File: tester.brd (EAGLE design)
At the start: 56 x 67 mm, 73 parts, among them IC1 ATmega8/88/168, K1 NA 05W K, M1 SP6000C-180, P1 250, P2 10k lin, Q1 BC847CSMD, Q2 BC847CSMD, Q3 BC328-40, Q4 8,000 MHz, Q5 BC847CSMD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

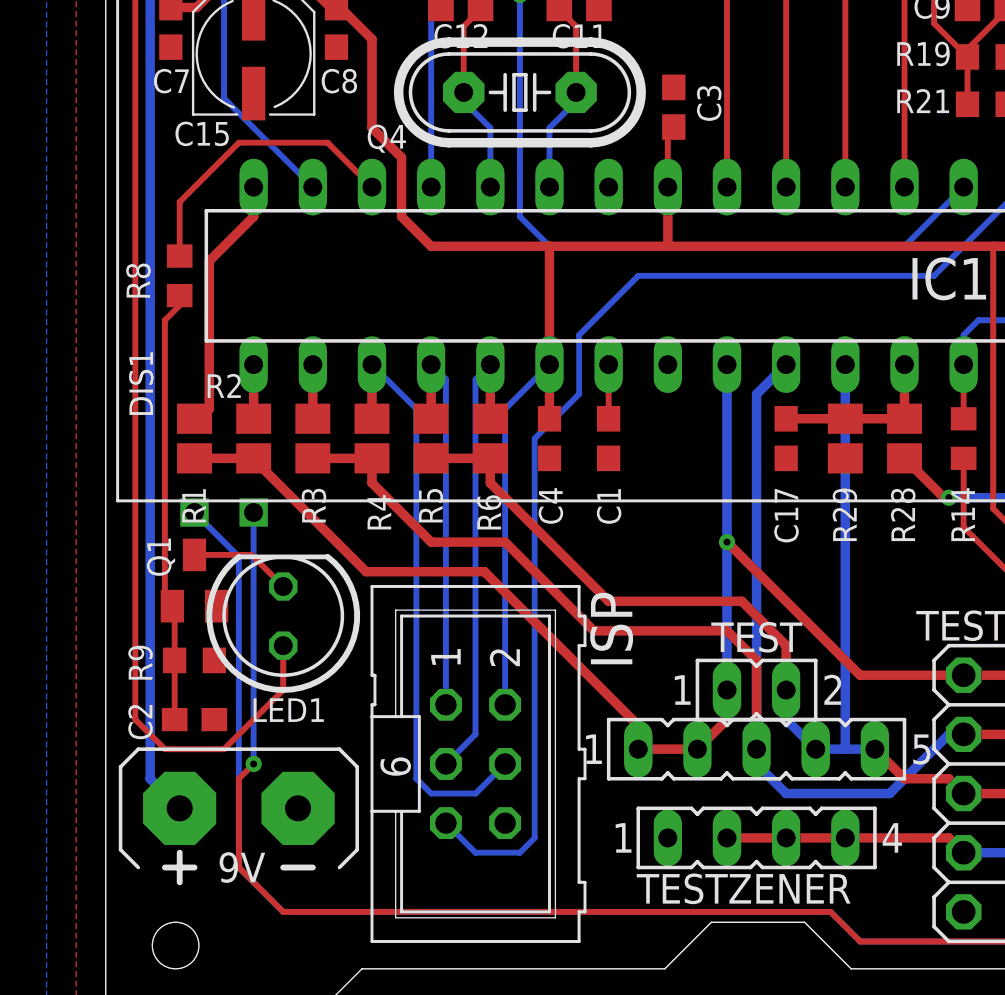
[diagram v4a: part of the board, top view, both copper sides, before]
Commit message: rearranged some parts, variant without pwm
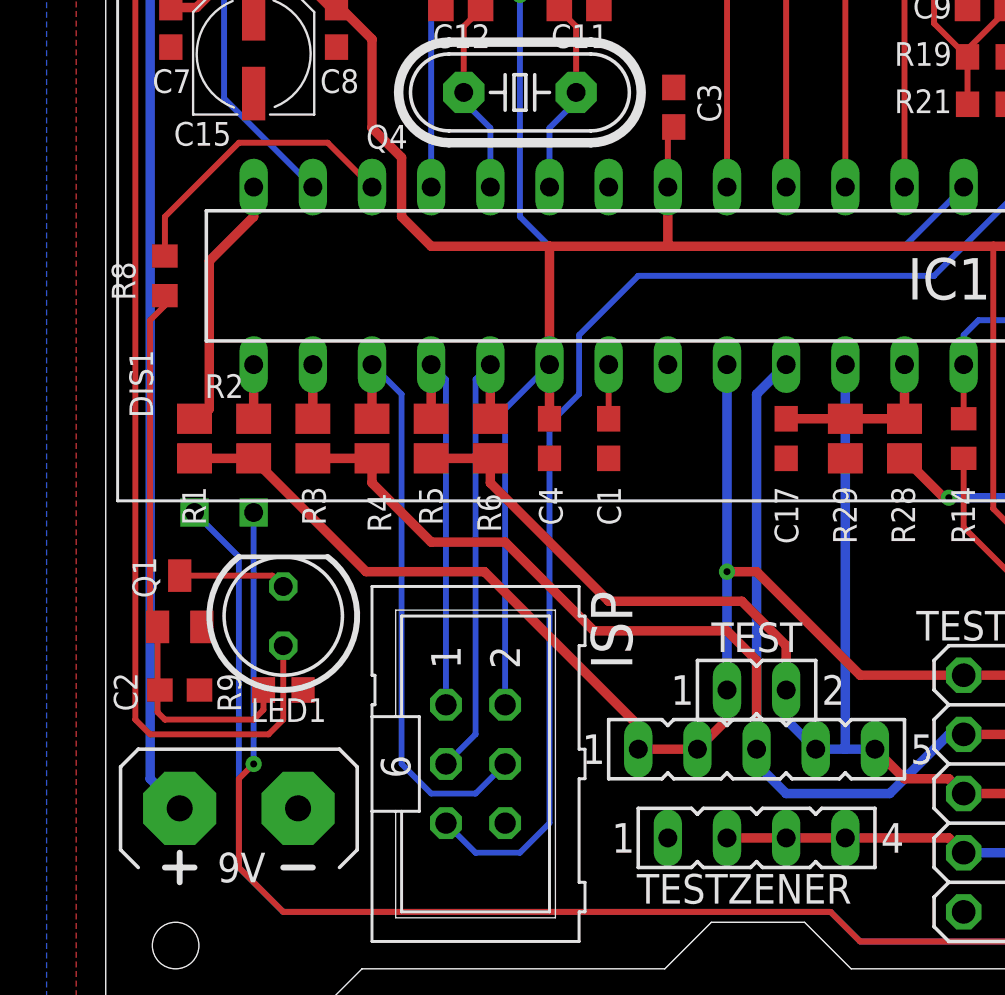
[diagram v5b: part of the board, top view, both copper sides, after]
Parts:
- moved R9 4.02 mm to (7.62, 14.0)
- moved C2 1.42 mm to (3.17, 14.0)
- moved Q1 1.09 mm to (3.17, 17.8)
- moved R8 0.63 mm to (2.54, 31.8)
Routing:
- net N$35: track 18.6 -> 24.1 mm
- net PC0: track 64.8 -> 64.3 mm

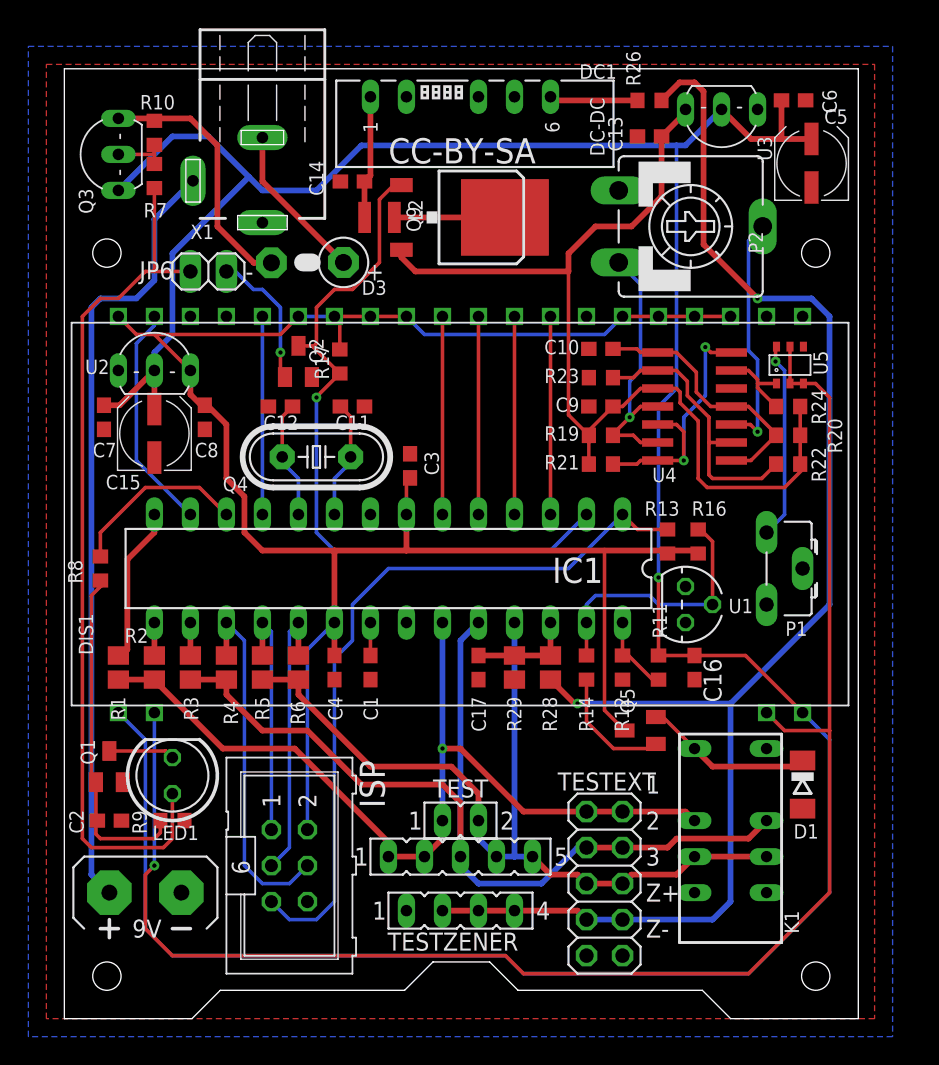
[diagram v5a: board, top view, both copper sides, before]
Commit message: smd for q3
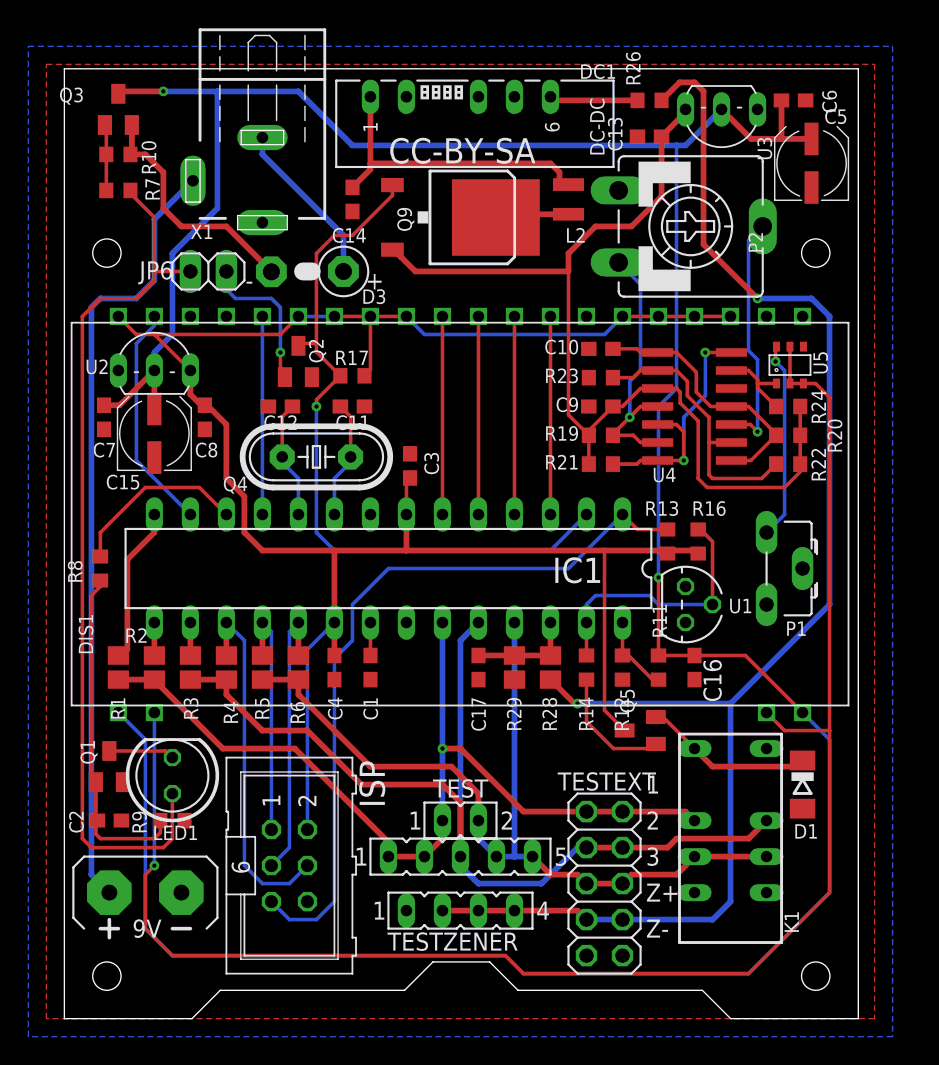
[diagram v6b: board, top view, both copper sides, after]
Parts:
- C13, C8: value X7R 10u -> 10u
- C6, C7: value X7R 1u -> 100n
- Q3: value BC328-40 -> BC807-40SMD; device transistor-pnp:TO92-EBC -> transistor-pnp:SOT23-BEC
- moved L2 13.4 mm to (35.6, 57.8), turned to 90 degrees
- moved Q3 3.42 mm to (3.81, 64.1), turned to 0 degrees
- moved R10 2.96 mm to (3.81, 61.0), turned to 180 degrees
- moved R7 2.74 mm to (3.81, 58.4), turned to 180 degrees
- moved R17 1.35 mm to (20.3, 45.3), turned to 0 degrees
- moved C14 1.27 mm to (20.3, 57.8), turned to 270 degrees
- moved D3 0.64 mm to (17.1, 52.7)
- moved Q9 0.63 mm to (27.9, 56.5)
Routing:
- net N$25: track 8.69 -> 22.0 mm
- net N$24: track 7.80 -> 5.34 mm
- net V+: track 211.5 -> 213.8 mm, vias 1 -> 2
- net +5V: track 139.3 -> 141.2 mm
- net N$5: track 18.5 -> 17.0 mm
- net N$21: track 61.7 -> 62.6 mm
- net N$33: track 3.89 -> 4.66 mm
- net N$3: track 9.90 -> 10.6 mm
- net N$11: track 11.2 -> 11.8 mm
- net N$7: track 19.8 -> 19.3 mm

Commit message: power lcd bg led in series
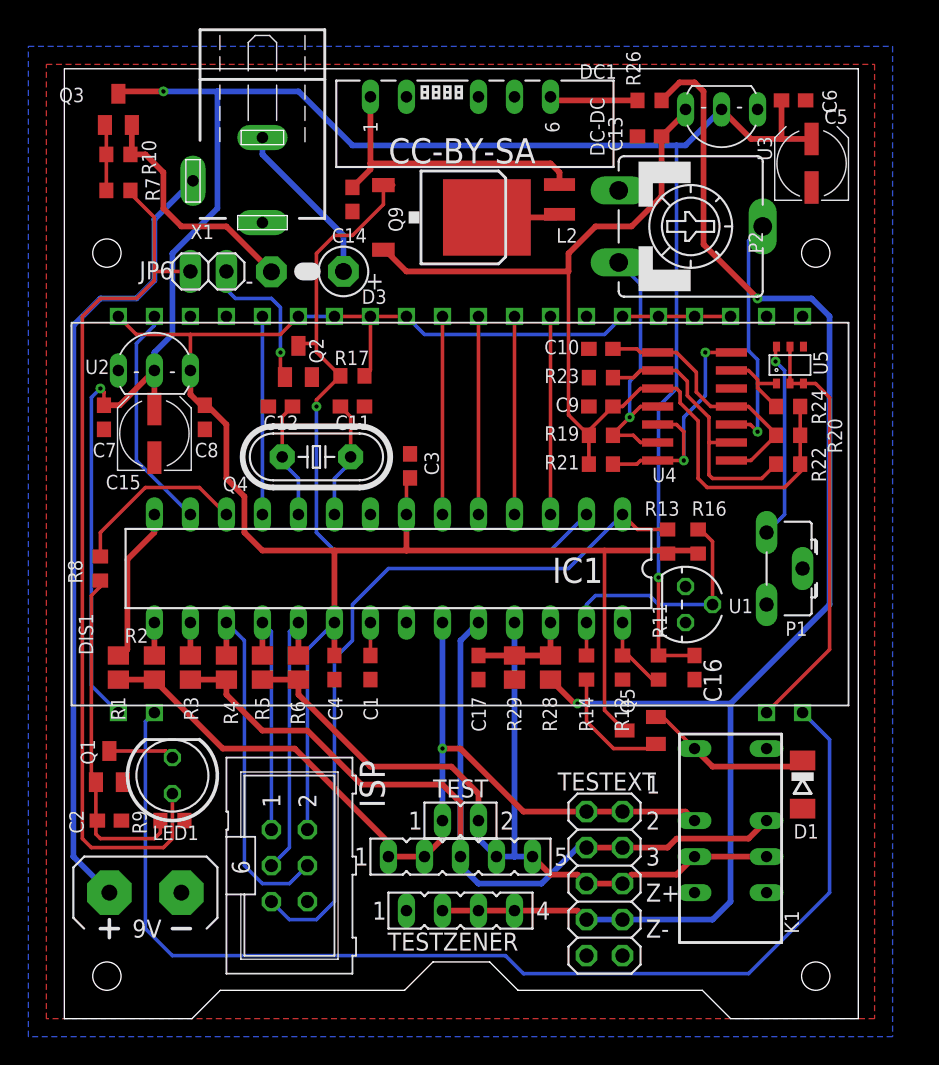
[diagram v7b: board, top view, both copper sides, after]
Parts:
- moved L2 0.64 mm to (34.9, 57.8)
- moved Q9 0.64 mm to (27.3, 56.5)
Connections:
- removed net N$18: DIS1.19, DIS1.2, U5.2, U5.3, U5.5
- new net N$10: DIS1.19, U5.2, U5.3, U5.5
- new net N$2: DIS1.2, DIS1.20
- net V+: no longer DIS1.20
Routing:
- net N$18: track 113.1 -> 0.00 mm, vias 1 -> 0
- net N$2: track 0.00 -> 80.9 mm
- net V+: track 213.8 -> 148.2 mm, vias 2 -> 3
- net N$10: track 0.00 -> 29.9 mm
- net N$9: track 55.2 -> 56.2 mm
- net +5V: track 141.2 -> 140.1 mm
- net +5V/2: track 71.2 -> 71.8 mm
- net N$25: track 22.0 -> 21.4 mm

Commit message: adjusted 1702 filter caps
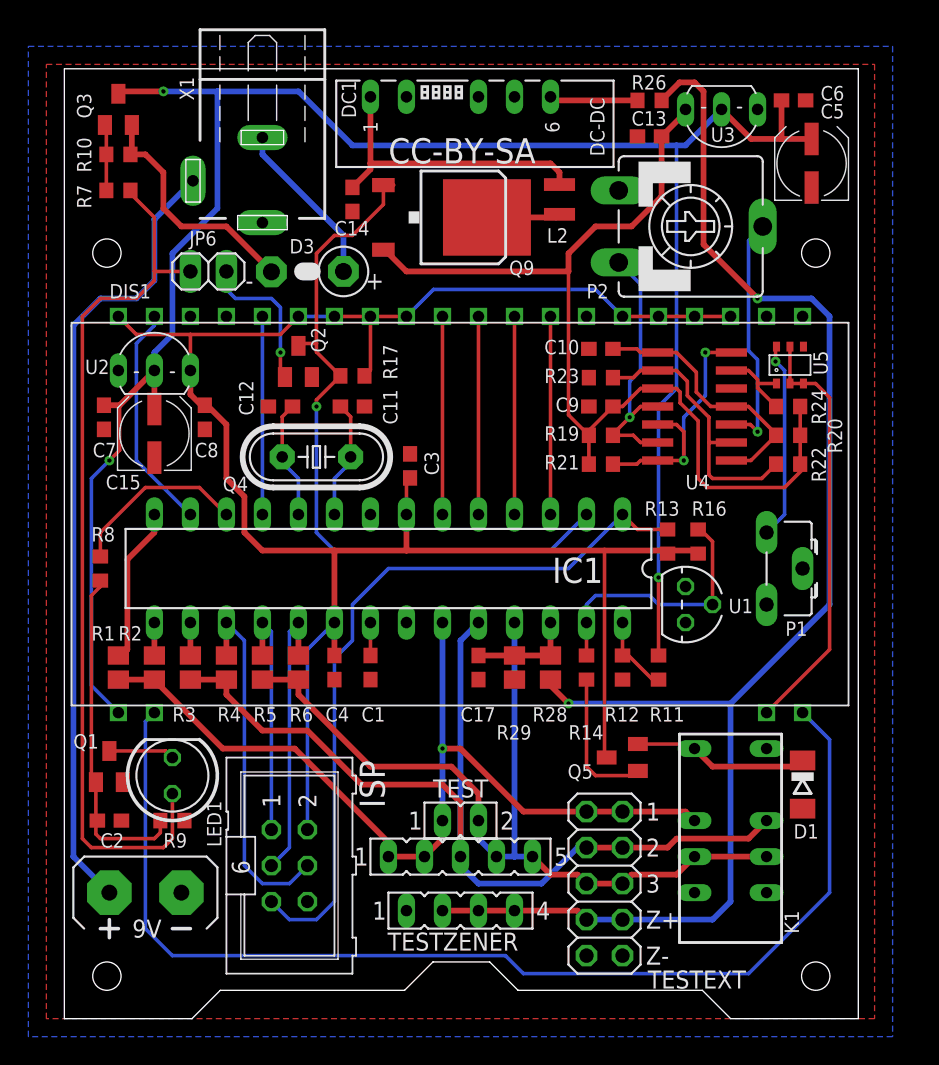
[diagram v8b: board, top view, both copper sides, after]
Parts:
- removed C16: 100n, rcl:C0603
- C13, C8: value 10u -> 1u
- C6, C7: value 100n -> 1u
- LED1: value POWER LED -> POWER
- moved Q5 2.29 mm to (39.4, 18.4)
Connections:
- net GND: no longer C16.2
- net V+: no longer C16.1
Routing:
- net V+: track 148.2 -> 143.8 mm
- net +5V: track 140.1 -> 142.0 mm
- net N$22: track 8.78 -> 10.2 mm
